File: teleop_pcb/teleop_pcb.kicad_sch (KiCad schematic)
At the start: 11 parts

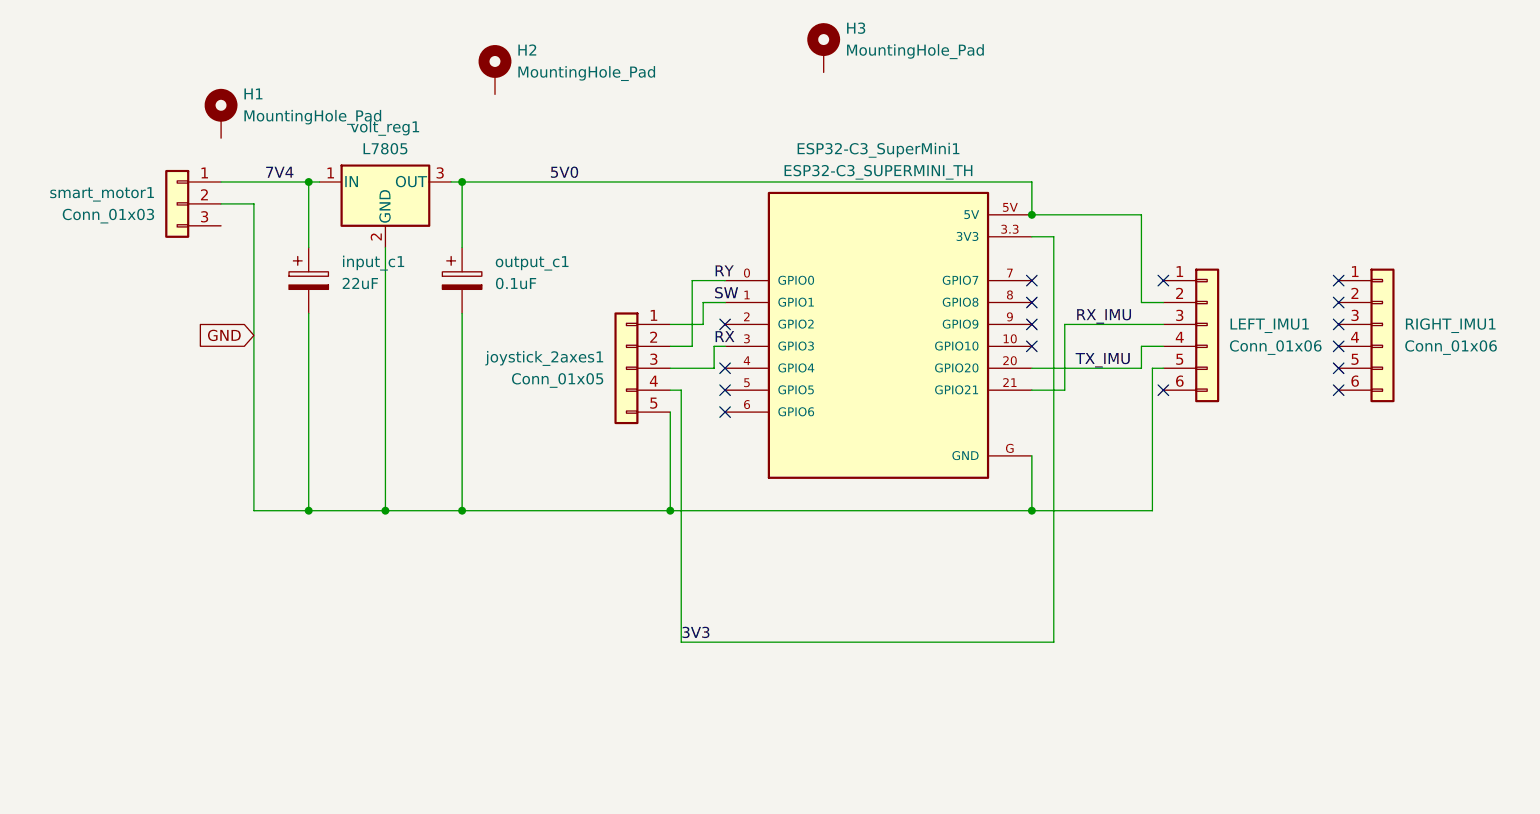
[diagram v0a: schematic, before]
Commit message: added pin socket rows for teleop pcb
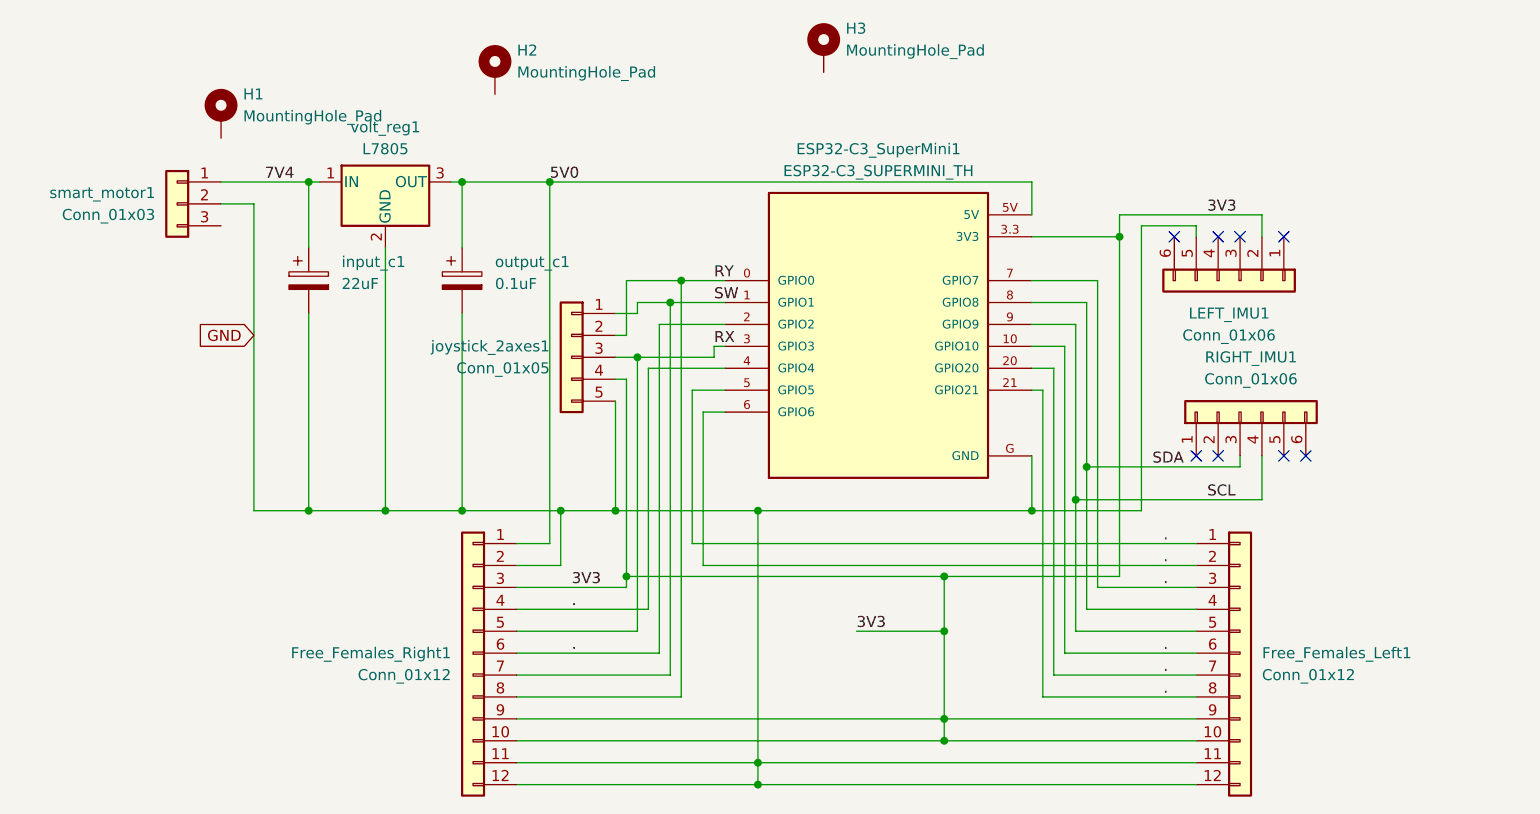
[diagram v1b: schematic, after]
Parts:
- added Free_Females_Left1, Free_Females_Right1: Conn_01x12, Connector_PinSocket_2.54mm:PinSocket_1x12_P2.54mm_Vertical, symbol Connector_Generic:Conn_01x12
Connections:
- net 3V3: now also LEFT_IMU1.2 (VCC), Free_Females_Left1.10 (Pin_10), Free_Females_Left1.9 (Pin_9), Free_Females_Right1.10 (Pin_10), Free_Females_Right1.3 (Pin_3), Free_Females_Right1.9 (Pin_9)
- net 5V0: now also Free_Females_Right1.1 (Pin_1); no longer LEFT_IMU1.2 (VCC)
- net GND: now also Free_Females_Left1.11 (Pin_11), Free_Females_Left1.12 (Pin_12), Free_Females_Right1.11 (Pin_11), Free_Females_Right1.12 (Pin_12), Free_Females_Right1.2 (Pin_2)
- net RX: now also Free_Females_Right1.5 (Pin_5)
- net RY: now also Free_Females_Right1.8 (Pin_8)
- net SW: now also Free_Females_Right1.7 (Pin_7)
- net SDA: now reaches RIGHT_IMU1.3 (Pin_3)
- net SDA: now also ESP32-C3_SuperMini1.8 (GPIO8), Free_Females_Left1.4 (Pin_4)
- net SCL: now reaches RIGHT_IMU1.4 (Pin_4)
- net SCL: now also ESP32-C3_SuperMini1.9 (GPIO9), Free_Females_Left1.5 (Pin_5)
- net .: now reaches ESP32-C3_SuperMini1.10 (GPIO10)
- net .: now also ESP32-C3_SuperMini1.2 (GPIO2), ESP32-C3_SuperMini1.20 (GPIO20), ESP32-C3_SuperMini1.21 (GPIO21), ESP32-C3_SuperMini1.4 (GPIO4), ESP32-C3_SuperMini1.5 (GPIO5), ESP32-C3_SuperMini1.6 (GPIO6), ESP32-C3_SuperMini1.7 (GPIO7), Free_Females_Left1.1 (Pin_1), Free_Females_Left1.2 (Pin_2), Free_Females_Left1.3 (Pin_3), Free_Females_Left1.6 (Pin_6), Free_Females_Left1.7 (Pin_7), Free_Females_Left1.8 (Pin_8), Free_Females_Right1.4 (Pin_4), Free_Females_Right1.6 (Pin_6)
- net RX_IMU: no longer names the net of LEFT_IMU1.3 (RX)
- net RX_IMU: no longer ESP32-C3_SuperMini1.21 (GPIO21)
- net TX_IMU: no longer names the net of LEFT_IMU1.4 (TX)
- net TX_IMU: no longer ESP32-C3_SuperMini1.20 (GPIO20)
- no-connect marks 16 -> 8
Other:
- moved on the sheet: LEFT_IMU1, RIGHT_IMU1, joystick_2axes1
